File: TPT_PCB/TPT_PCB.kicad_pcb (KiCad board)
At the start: 2 copper layers, 69.4 x 66.2 mm, 55 parts, among them J1 Conn_01x04, J2 Conn_01x04, J3 Conn_01x04, J4 Conn_01x04, J5 Conn_01x04, J6 SWD, J7 Power, J8 Conn_01x06, SW1 SW_Push, U1 TCA9548APWR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

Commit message: 修正PCB文字層錯誤
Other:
- board text added: "+"

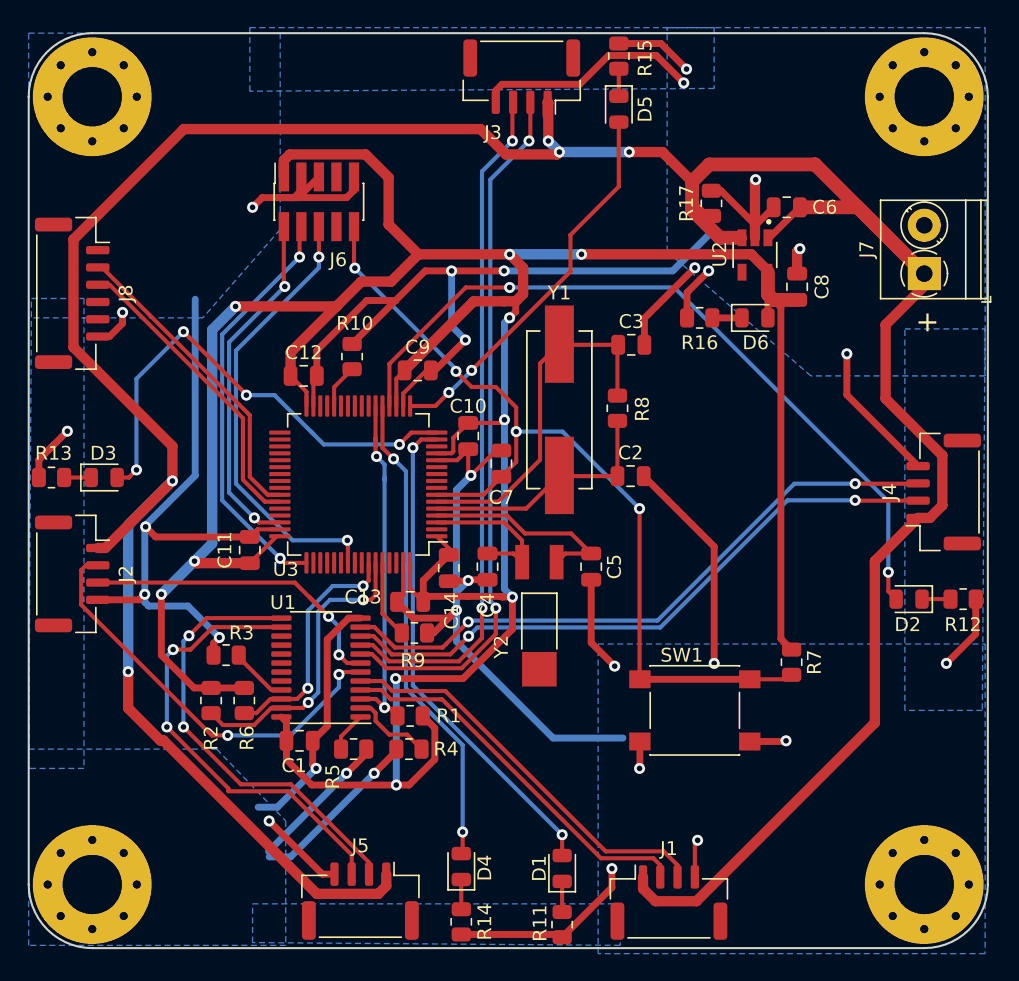
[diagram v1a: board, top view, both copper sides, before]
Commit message: change SWD connector add layout TODO list
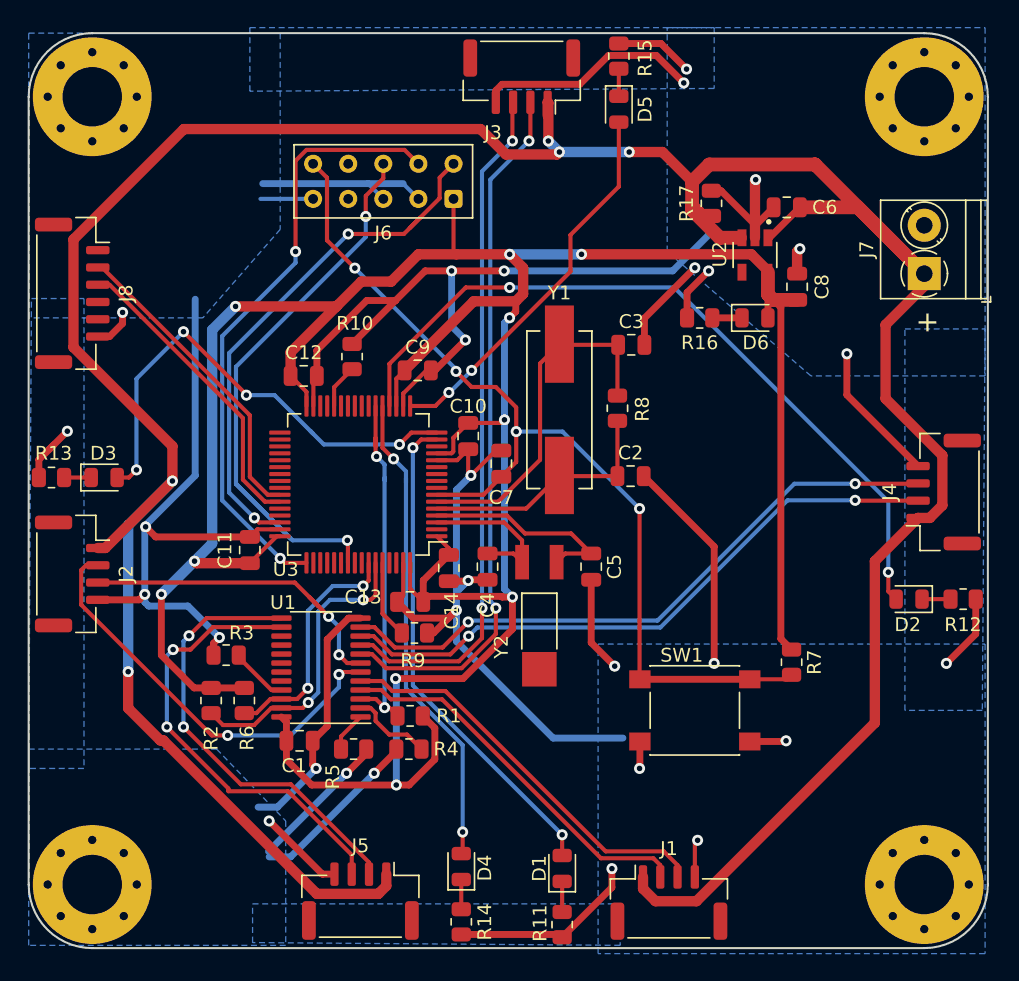
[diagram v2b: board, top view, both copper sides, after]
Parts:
- J6: footprint Connector_PinSocket_1.27mm:PinSocket_2x05_P1.27mm_Vertical_SMD -> Connector_Samtec_HLE_THT:Samtec_HLE-105-02-xx-DV-TE_2x05_P2.54mm_Horizontal
- moved J6 9.74 mm to (154.9, 72.4), turned to 180 degrees
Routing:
- net /SWCLK: track 30.1 -> 44.4 mm
- net /SWDIO: track 25.5 -> 38.5 mm
- net +3V3: track 240.6 -> 228.6 mm
- net /SWO: track 33.3 -> 44.6 mm
- net /NRST: track 64.3 -> 70.2 mm
- net GND: track 325.8 -> 328.6 mm, vias 30 -> 29
